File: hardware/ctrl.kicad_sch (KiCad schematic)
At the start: 21 parts, among them J1 Conn_01x06, J3 USB_C_Receptacle_USB2.0_16P, Q1 BC817W, Q2 BC817W, U1 ESP32-WROOM-32E, U9 ESP32-C3-WROOM-02

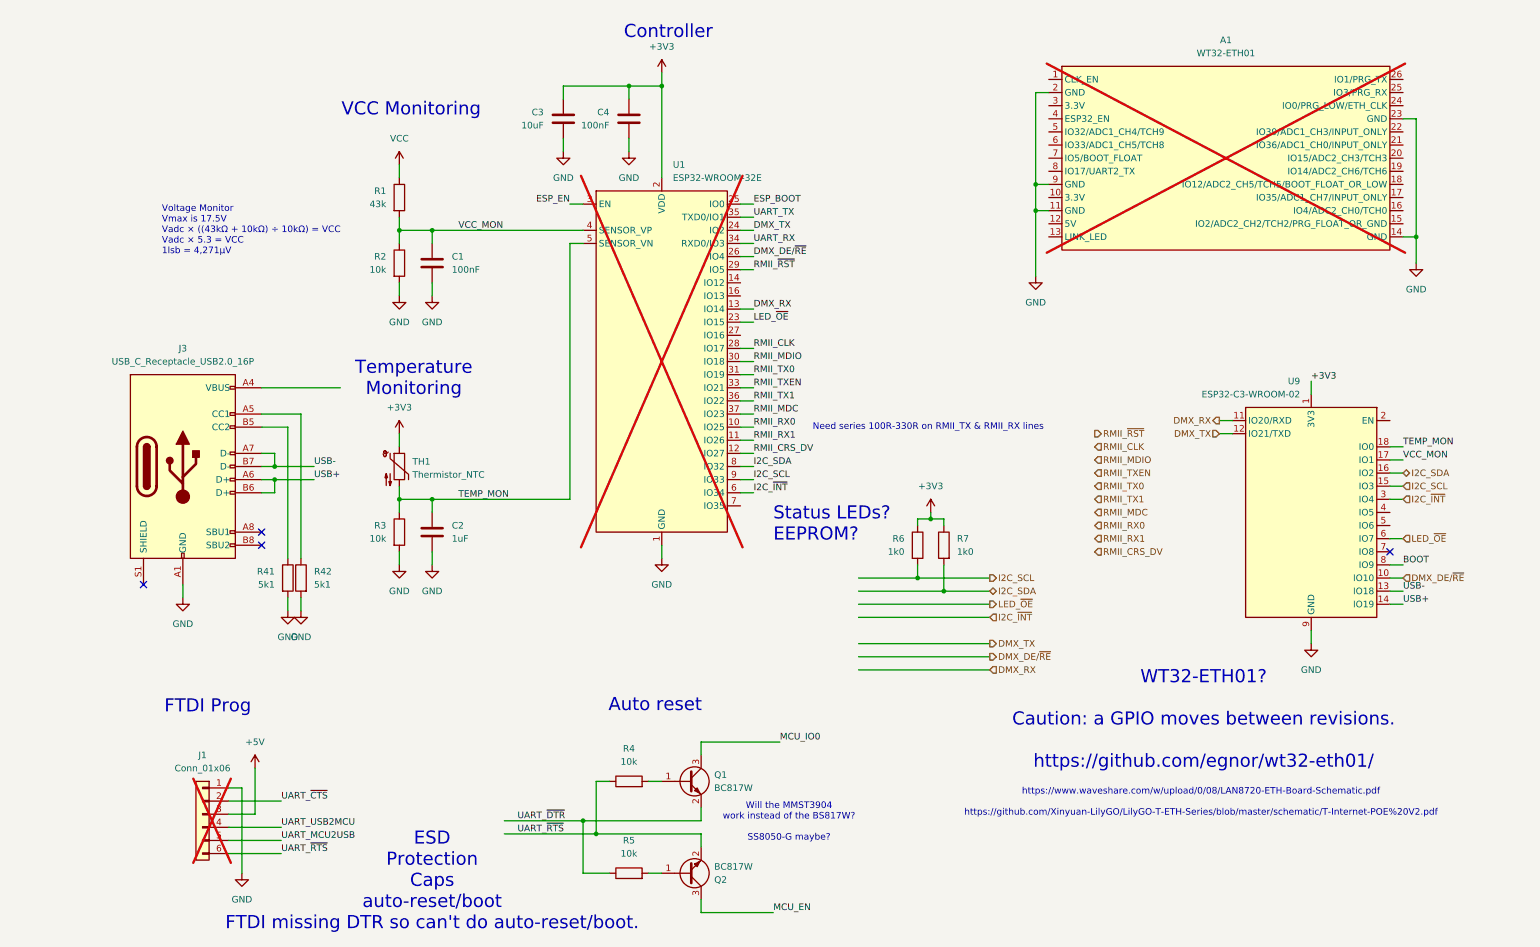
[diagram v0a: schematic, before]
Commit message: removed Art-Net
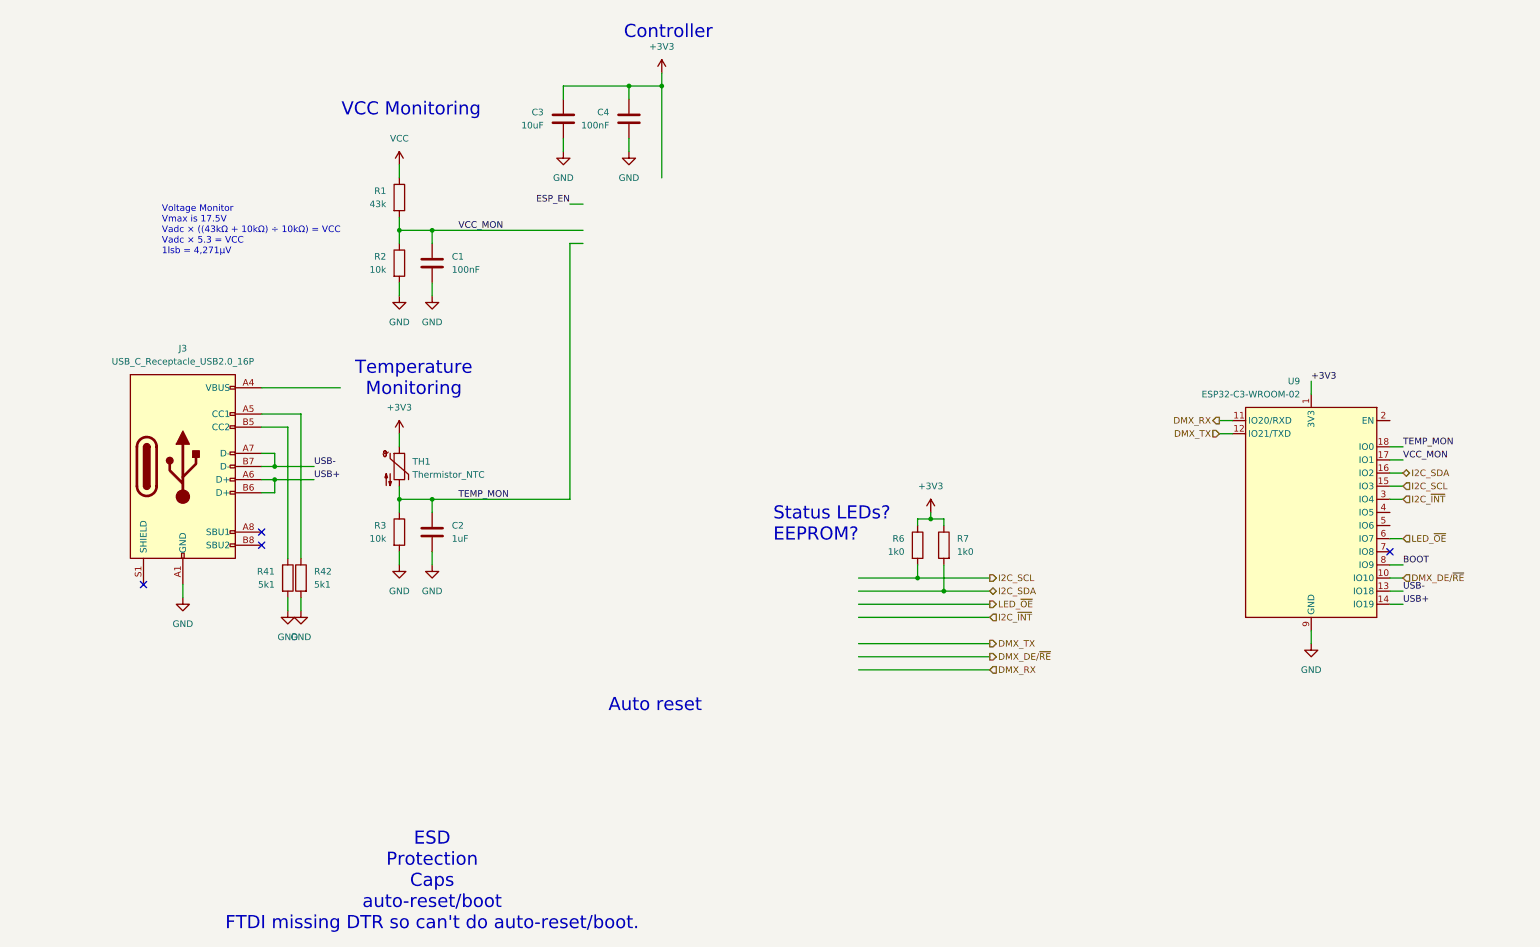
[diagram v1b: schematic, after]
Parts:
- removed A1: WT32-ETH01, Pinski1_parts:WT32-ETH01, symbol Pinski1_Parts:WT32-ETH01
- removed J1: Conn_01x06, Connector_PinHeader_2.54mm:PinHeader_1x06_P2.54mm_Vertical, symbol Connector_Generic:Conn_01x06
- removed Q1, Q2: BC817W, Package_TO_SOT_SMD:SOT-323_SC-70, symbol Transistor_BJT:BC817W
- removed R4, R5: 10k, Resistor_SMD:R_0603_1608Metric, symbol Device:R
- removed U1: ESP32-WROOM-32E, RF_Module:ESP32-WROOM-32D, symbol RF_Module:ESP32-WROOM-32E
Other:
- note removed: "FTDI Prog"
- note removed: "Need series 100R-330R on RMII_TX & RMII_RX lines"
- note removed: "WT32-ETH01? Caution: a GPIO moves between revisions. https://github.com/egnor/wt32-eth01/"
- note removed: "Will the MMST3904 work instead of the BS817W? SS8050-G maybe?"
- note removed: "https://www.waveshare.com/w/upload/0/08/LAN8720-ETH-Board-Schematic.pdf https://github.com/Xinyuan-LilyGO/LilyGO-T-ETH-Series/blob/master/schematic/T-Internet-POE%20V2.pdf"

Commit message: clean up
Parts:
- added C25, C26: 100nF, Capacitor_SMD:C_0603_1608Metric, symbol Device:C
- added C27: 10uF, Capacitor_SMD:C_0805_2012Metric, symbol Device:C
- added D5: SS34, Diode_SMD:D_SMA, symbol Device:D_Schottky
- added D6: 1N4148, symbol Device:D
- added R41, R42: 10k, Resistor_SMD:R_0603_1608Metric, symbol Device:R
- added SW2: SW_Push, Button_Switch_SMD:SW_SPST_B3U-1000P, symbol Switch:SW_Push
- renumbered C3 to C1, C4 to C2, C2 to C3, C1 to C4, J3 to J1, R41 to R1, R42 to R2, R6 to R4, R7 to R5, R1 to R6, R2 to R7, U9 to U1
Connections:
- net +3V3: now also R41.1, R42.2
- net BOOT: now also C27.1, D6.2 (A)
- net DMX_DE/~{RE}: now also U1.5 (IO6); no longer U1.10 (IO10)
- net ESP_EN: now also U1.2 (EN), C26.1, D6.1 (K), R41.2, SW2.2
- net GND: now also C25.2, C26.2, C27.2, SW2.1
- net I2C_SCL: now also R5.2; no longer R4.2
- net I2C_SDA: now also R4.2; no longer R5.2
- net at J1.A4 (VBUS), J1.A9 (VBUS), J1.B4 (VBUS)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: now also C25.1, D5.2 (A)
- net at U1.7 (IO8): now also R42.1
- net VCC renamed VDC
- net VDC: now also D5.1 (K)
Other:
- note added: "USB Programming"
- note removed: "ESD Protection Caps auto-reset/boot FTDI missing DTR so can't do auto-reset/boot."
- moved on the sheet: C1, C2, C3, C4, J1, R1, R2, R3, R4, R5, R6, R7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

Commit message: updating readme
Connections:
- net BOOT renamed ESP_~{BOOT}
- net ESP_EN renamed ESP_~{RST}
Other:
- note added: "Short press resets the ESP32 Long press resets the ESP32 and puts it in bootloader mode"
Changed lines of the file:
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@@
+		)
+	)
+	(text "Short press resets the ESP32\nLong press resets the ESP32\nand puts it in bootloader mode"
+		(exclude_from_sim no)
+		(at 45.72 161.798 0)
+		(effects
+			(font
+				(size 1.27 1.27)
+			)
+			(justify left bottom)
 		)
 	)
@@
 		)
 	)
-	(label "BOOT"
+	(label "ESP_~{BOOT}"
 		(at 85.09 135.89 0)
 		(effects
@@
 		)
 	)
-	(label "BOOT"
+	(label "ESP_~{BOOT}"
 		(at 161.29 102.87 0)
 		(effects
@@
 		)
 	)
-	(label "ESP_EN"
+	(label "ESP_~{RST}"
 		(at 52.07 135.89 0)
 		(effects
@@
 		)
 	)
-	(label "ESP_EN"
+	(label "ESP_~{RST}"
 		(at 161.29 74.93 0)
 		(effects

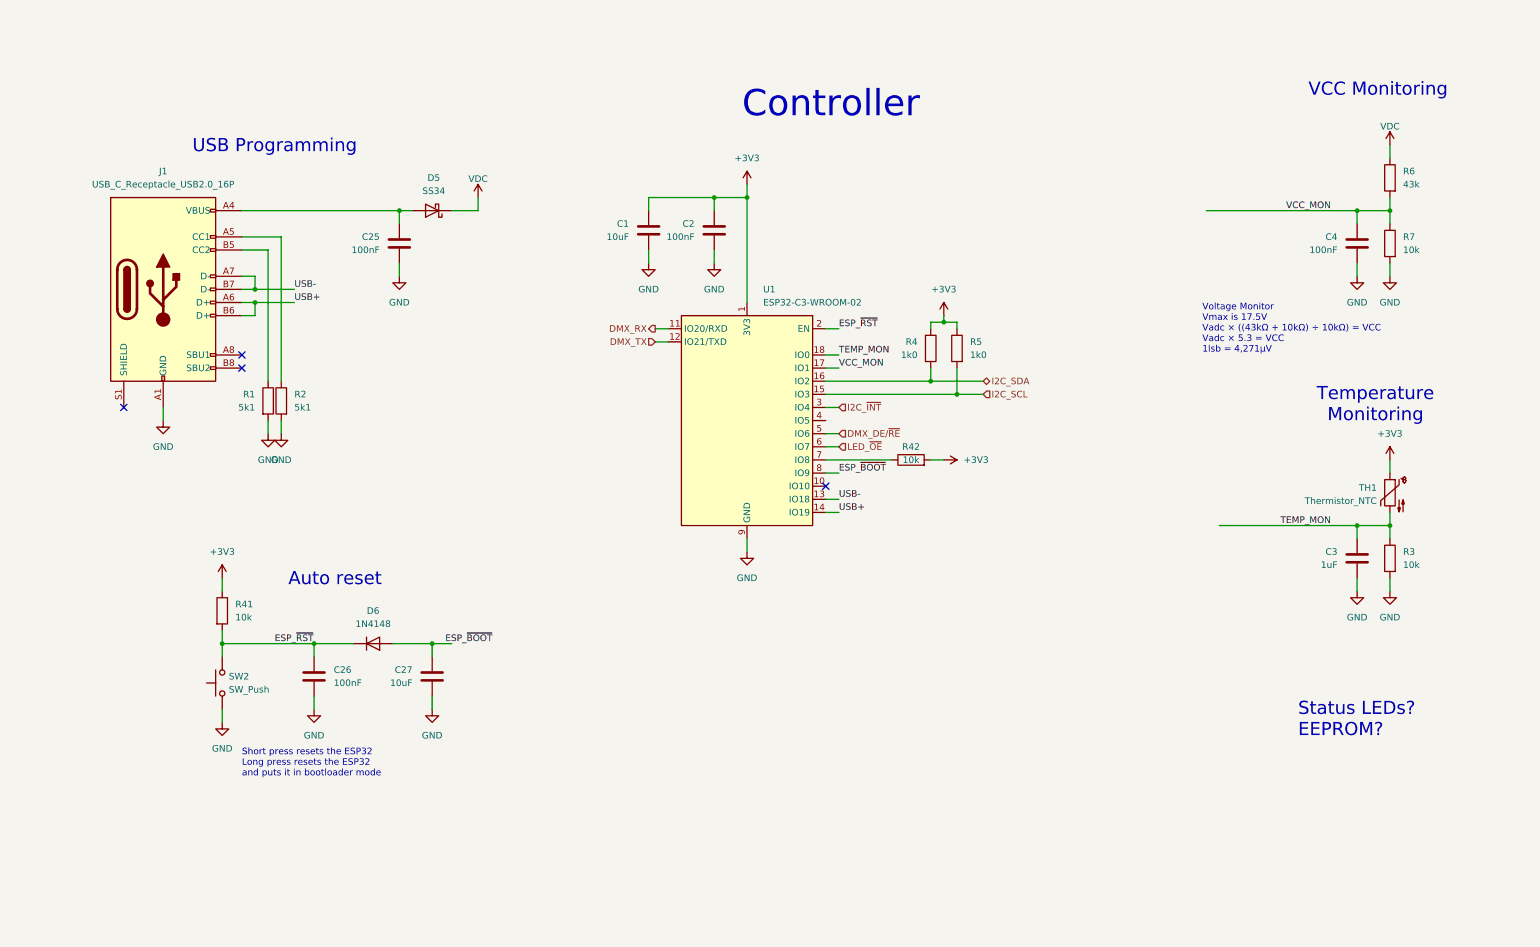
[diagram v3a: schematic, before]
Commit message: updating thermistor and GPIO expander
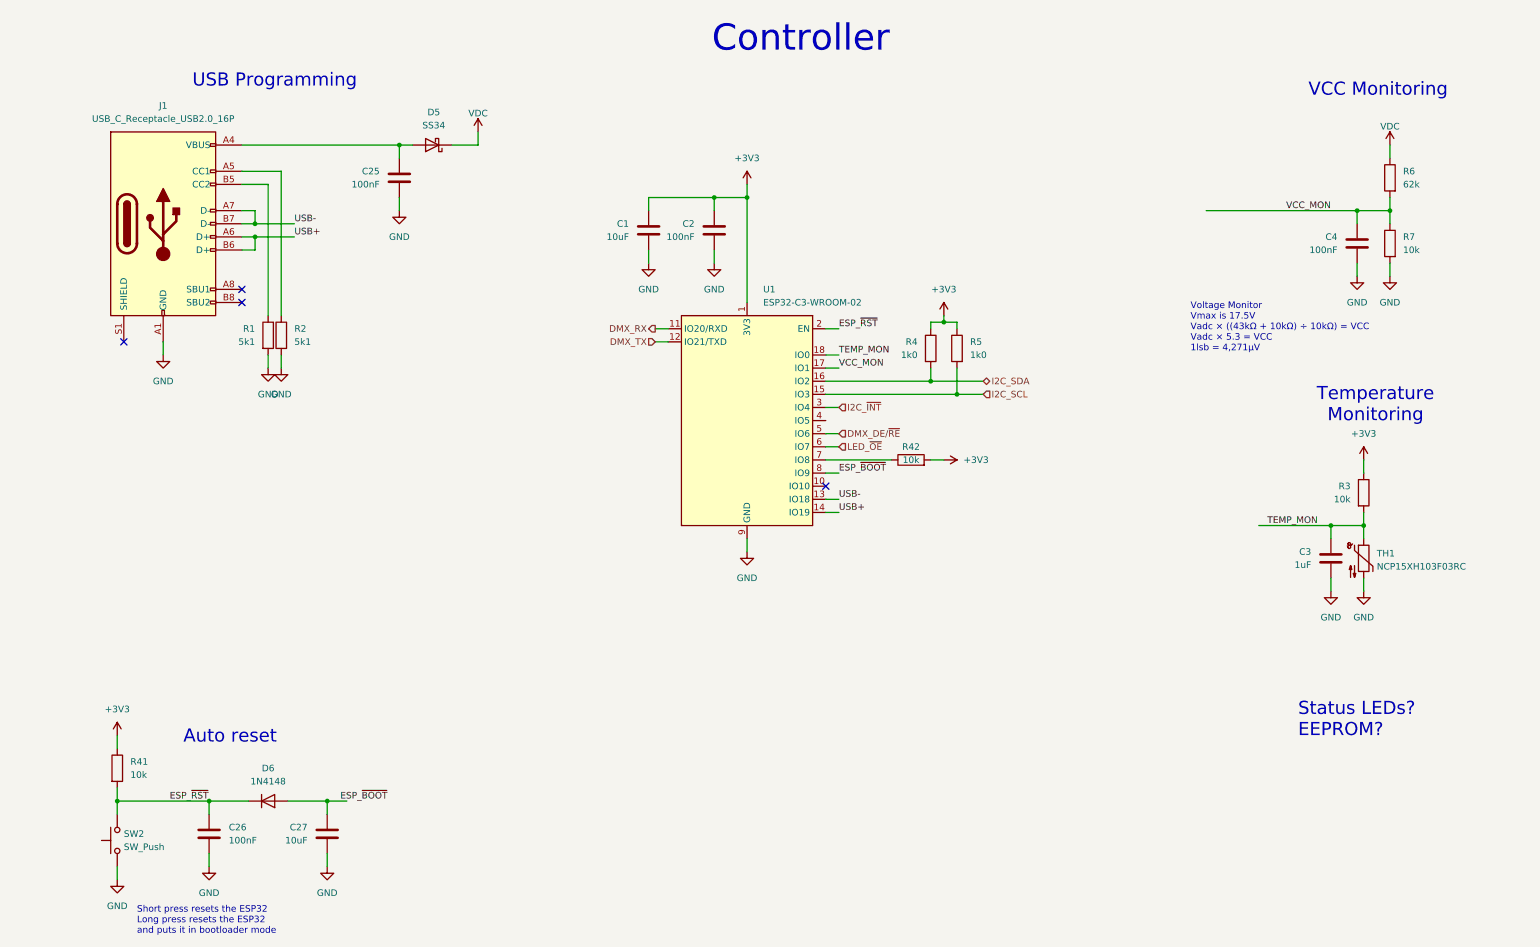
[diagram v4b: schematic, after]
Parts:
- R6: value 43k -> 62k
- TH1: value Thermistor_NTC -> NCP15XH103F03RC; LCSC (none) -> C77131; MFR (none) -> Murata Electronics; MPN (none) -> NCP15XH103F03RC
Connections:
- net +3V3: now also R3.1; no longer TH1.1
- net GND: now also TH1.2; no longer R3.2
- net TEMP_MON: now also R3.2, TH1.1; no longer R3.1, TH1.2
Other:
- moved on the sheet: C25, C26, C27, C3, D5, D6, J1, R1, R2, R41, SW2, TH1

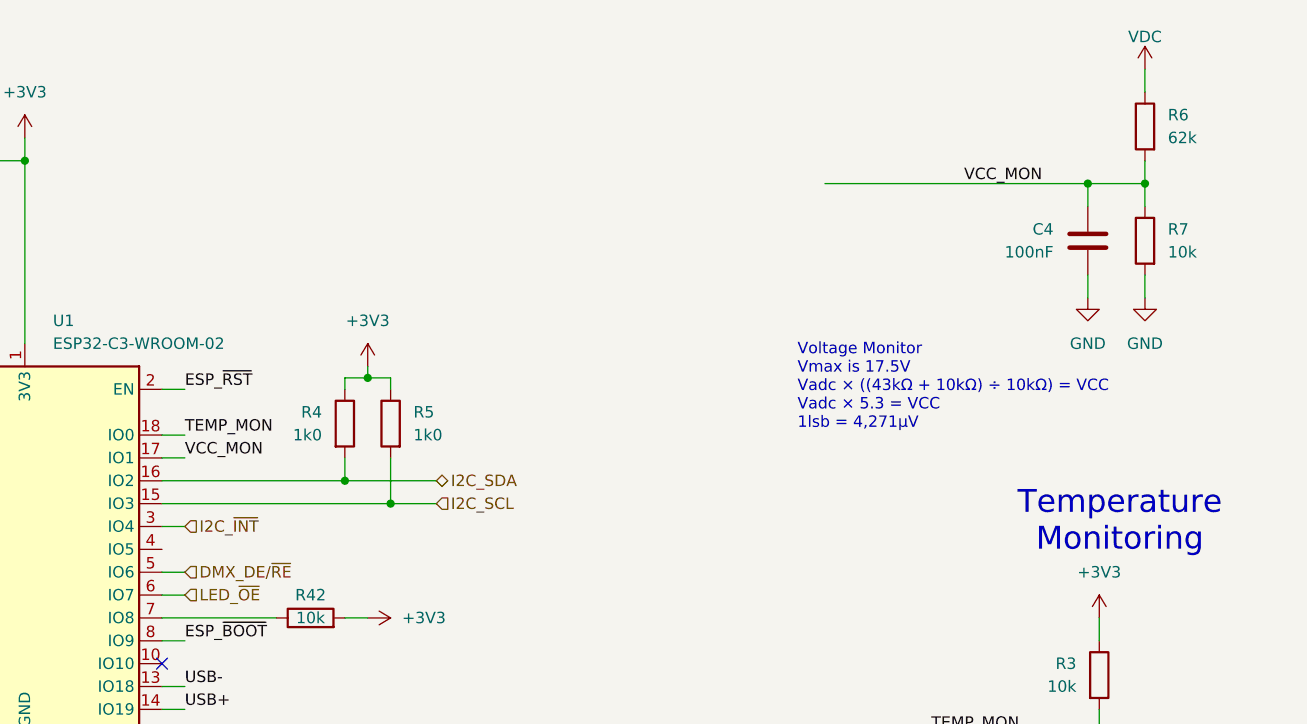
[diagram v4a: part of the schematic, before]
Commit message: adding snubbers, starting placement
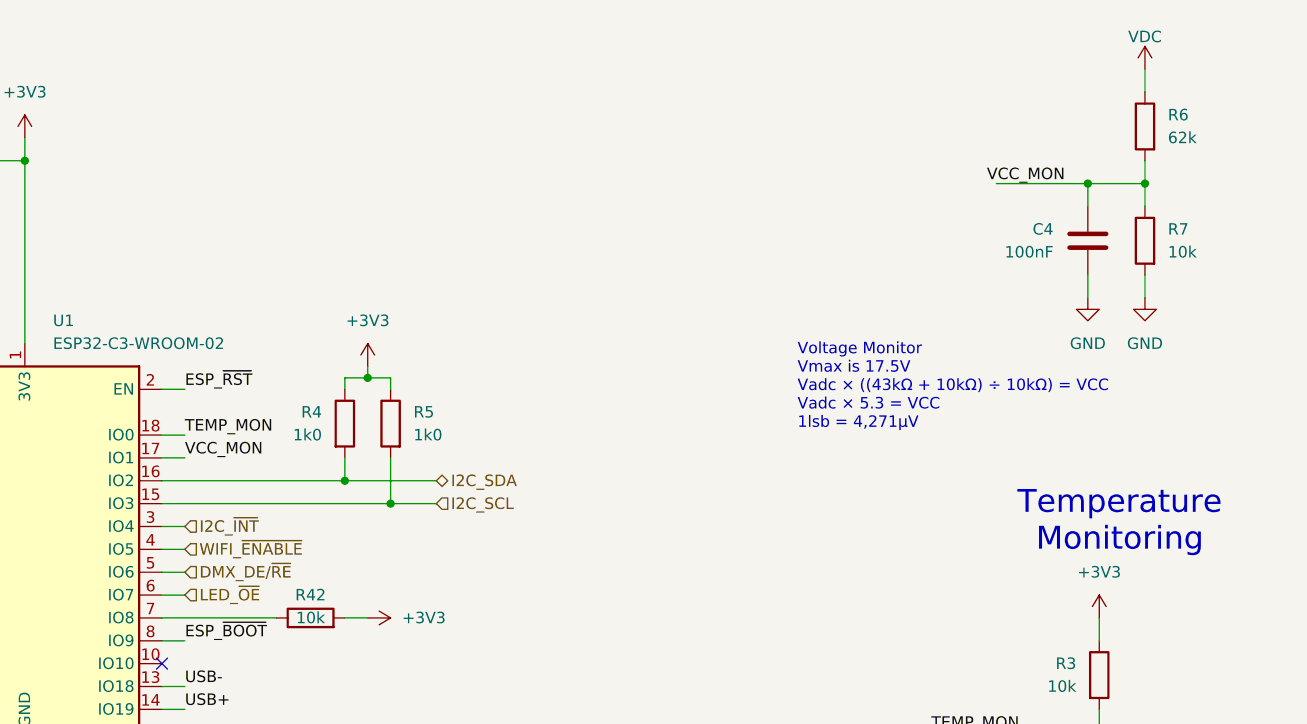
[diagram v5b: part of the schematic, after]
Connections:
- net WIFI_~{ENABLE}: now reaches U1.4 (IO5)
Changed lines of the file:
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@@
-	(wire
-		(pts
-			(xy 261.62 52.07) (xy 232.41 52.07)
-		)
-		(stroke
-			(width 0)
-			(type default)
-		)
-	)
 	(wire
 		(pts
@@
 	(wire
 		(pts
+			(xy 261.62 52.07) (xy 267.97 52.07)
+		)
+		(stroke
+			(width 0)
+			(type default)
+		)
+	)
+	(wire
+		(pts
 			(xy 262.89 113.03) (xy 256.54 113.03)
 		)
@@
 	(wire
 		(pts
+			(xy 251.46 52.07) (xy 261.62 52.07)
+		)
+		(stroke
+			(width 0)
+			(type default)
+		)
+	)
+	(wire
+		(pts
 			(xy 53.34 44.45) (xy 53.34 72.39)
 		)
@@
 	(wire
 		(pts
+			(xy 158.75 92.71) (xy 161.29 92.71)
+		)
+		(stroke
+			(width 0)
+			(type default)
+		)
+	)
+	(wire
+		(pts
 			(xy 143.51 46.99) (xy 143.51 49.53)
 		)
@@
 		(pts
 			(xy 158.75 85.09) (xy 179.07 85.09)
-		)
-		(stroke
-			(width 0)
-			(type default)
-		)
-	)
-	(wire
-		(pts
-			(xy 267.97 52.07) (xy 261.62 52.07)
 		)
 		(stroke
@@
 	)
 	(label "VCC_MON"
-		(at 256.54 52.07 180)
+		(at 259.08 52.07 180)
 		(effects
 			(font
@@
 		(effects
 			(font
+				(size 1.27 1.27)
+			)
+			(justify left)
+		)
+	)
+	(hierarchical_label "WIFI_~{ENABLE}"
+		(shape input)
+		(at 161.29 92.71 0)
+		(effects
+			(font
